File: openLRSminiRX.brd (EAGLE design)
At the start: 20.2 x 21.8 mm, 19 parts, among them U1 ATMEGA328P, U2 V_REG_LDOSMD

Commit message: update, fully routed.
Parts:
- removed C4, C9: (no value), rcl:C0805
- removed U2: V_REG_LDOSMD, SparkFun-PowerIC:SOT23-5
- added FILTER-1: LFCN-490, minicircuits:FV1206
- added IC1: MCP1703CB, linear:SOT23
- added JP10: SCL, SparkFun-Connectors:1X01
- added JP11: VCC, SparkFun-Connectors:1X01
- added JP12: SBUS, SparkFun-Connectors:1X01
- added JP13, JP14, JP8: GND, SparkFun-Connectors:1X01
- added JP3: RSSI, SparkFun-Connectors:1X01
- added JP4: PPM, SparkFun-Connectors:1X01
- added JP5: TXD, SparkFun-Connectors:1X01
- added JP6: RXD, SparkFun-Connectors:1X01
- added JP7: VIN, SparkFun-Connectors:1X01
- added JP9: SDA, SparkFun-Connectors:1X01
- added R3, R7: (no value), SparkFun-Resistors:0805
- C1, C10, C5, C6: device rcl:C0805 -> SparkFun-Capacitors:0805
- JP1: value (none) -> ANT; device SparkFun-Connectors:1X05 -> SparkFun-Connectors:1X01
- JP2: value (none) -> ANTF; device SparkFun-Connectors:1X05 -> SparkFun-Connectors:1X01
- R1, R2, R4, R5, R6: device rcl:R0805 -> SparkFun-Resistors:0805
- moved JP1 22.1 mm to (19.8, 18.0)
- moved JP2 16.0 mm to (19.8, 13.0)
- moved R4 14.7 mm to (13.0, 15.7), turned to 180 degrees
- moved C6 8.70 mm to (5.84, 14.2)
- moved C10 5.57 mm to (2.03, 2.54), turned to 270 degrees
- moved R2 4.02 mm to (17.8, 6.86)
- moved R1 3.78 mm to (17.8, 4.83)
- moved LED1 3.70 mm to (14.0, 4.83)
- moved LED2 3.21 mm to (14.0, 6.35)
- moved R6 2.90 mm to (9.40, 14.2), turned to 180 degrees
- moved Q1 2.27 mm to (8.64, 17.0), turned to 270 degrees
- moved C1 2.18 mm to (13.0, 17.5), turned to 180 degrees
- moved U$1 0.76 mm to (9.40, 10.9)
- moved R5 0.51 mm to (14.0, 8.13)
- moved U1 0.51 mm to (7.11, 7.87)
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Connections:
- removed net DTR: C9.1
- removed net N$16: C4.1, U2.4
- new net N$1: FILTER-1.1, JP1.1, U$1.1
- new net N$4: FILTER-1.3, JP2.1
- new net N$5: JP4.1, R7.1
- net GND: now also FILTER-1.2, FILTER-1.4, JP13.1, JP14.1, JP8.1; no longer C4.2, U2.2
- net N$10: now also R3.2
- net N$18: no longer C9.2
- net PPM: now also R7.2
- net RSSI: now also JP3.1
- net RXD: now also JP6.1
- net SBUS: now also JP12.1
- net SCL: now also JP10.1; no longer JP2.2
- net SDA: now also JP9.1; no longer JP2.3
- net TXD: now also JP5.1
- net VCC: now also IC1.2, JP11.1, R3.1; no longer JP2.1, U2.5
- net VIN: now also IC1.3, JP7.1; no longer U2.1, U2.3
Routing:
- net VCC: track 0.00 -> 48.1 mm, vias 0 -> 4
- net TXD: track 0.00 -> 33.4 mm, vias 0 -> 3
- net N$17: track 0.00 -> 17.4 mm, vias 0 -> 2
- net N$10: track 0.00 -> 14.6 mm, vias 0 -> 1
- net PPM: track 0.00 -> 14.0 mm
- net N$11: track 0.00 -> 13.0 mm, vias 0 -> 3
- net SCL: track 0.00 -> 10.5 mm, vias 0 -> 1
- net RXD: track 0.00 -> 10.1 mm, vias 0 -> 1
- net N$3: track 0.00 -> 9.38 mm
- net SBUS: track 0.00 -> 8.38 mm
- net N$9: track 0.00 -> 8.22 mm, vias 0 -> 1
- net N$19: track 0.00 -> 7.89 mm, vias 0 -> 2
- net SDA: track 0.00 -> 7.15 mm, vias 0 -> 1
- net RSSI: track 0.00 -> 5.74 mm
- net N$2: track 0.00 -> 5.64 mm
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- added copper zone on layer 1, net GND
- added copper zone on layer 16, net GND
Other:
- board size 20.2 x 21.8 mm -> 21.3 x 21.8 mm

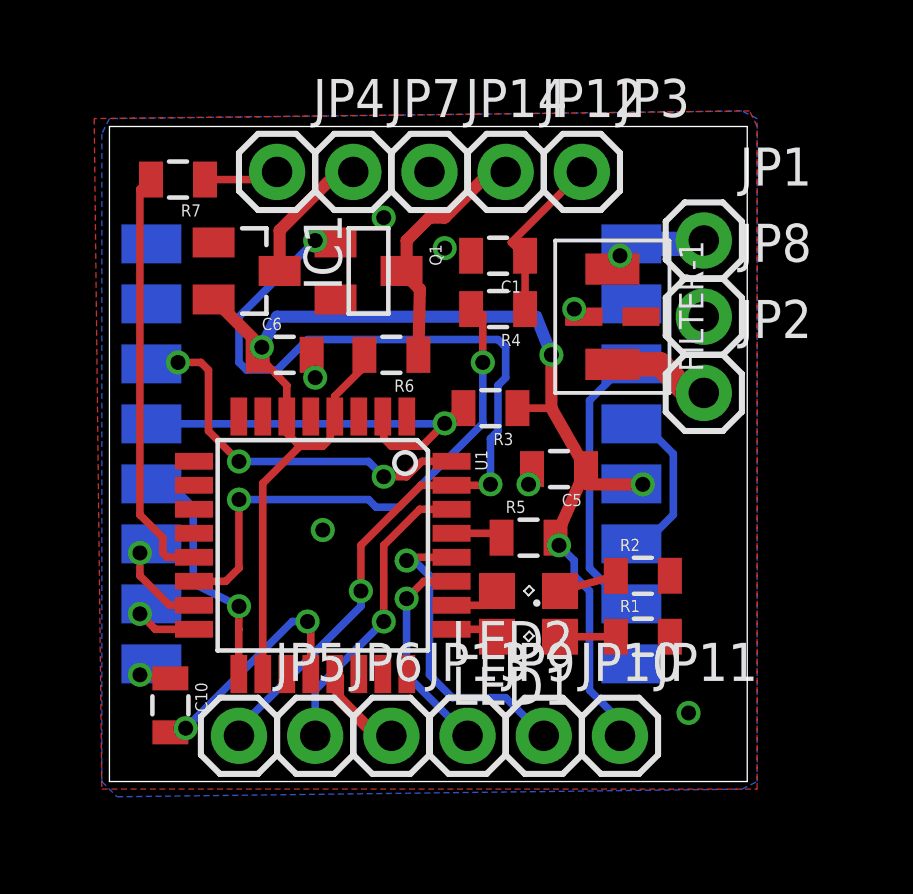
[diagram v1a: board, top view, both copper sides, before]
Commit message: updates (fix RSSI output pin)
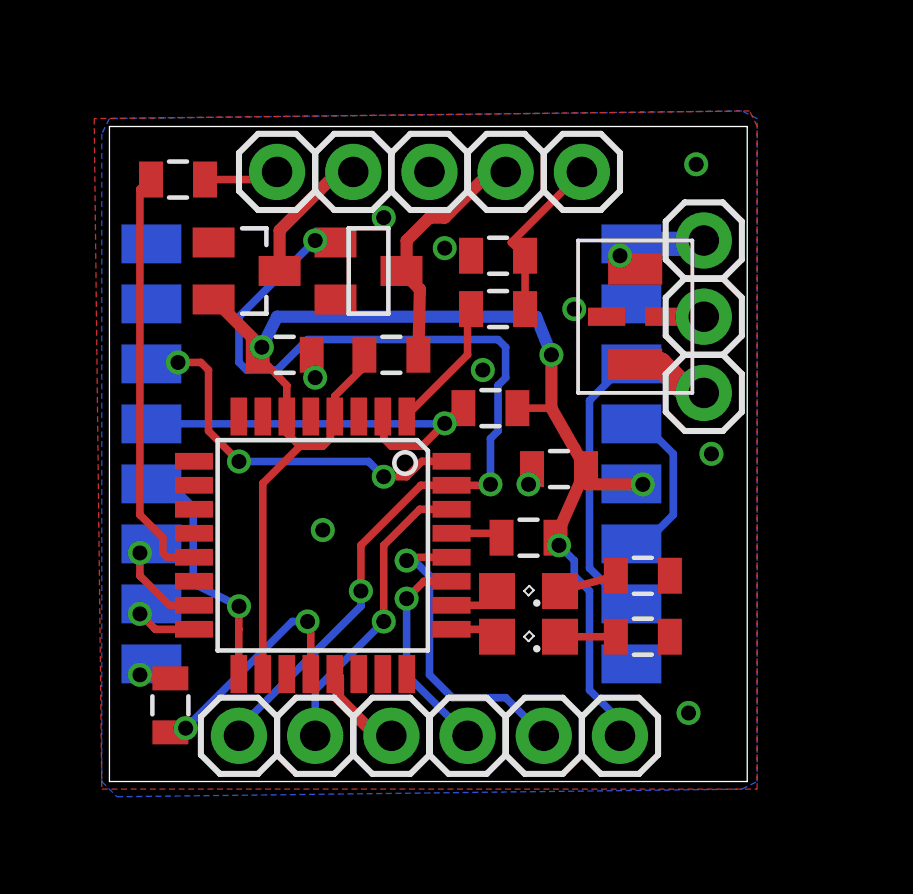
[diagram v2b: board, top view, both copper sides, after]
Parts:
- moved FILTER-1 0.76 mm to (17.5, 15.5)
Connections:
- removed net N$17: R4.2, U1.14
- new net N$6: R4.2, U1.1
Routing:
- net N$17: track 17.4 -> 0.00 mm, vias 2 -> 0
- net N$6: track 0.00 -> 4.47 mm
- net N$4: track 3.44 -> 2.68 mm
- net GND: vias 8 -> 11

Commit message: cleanups
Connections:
- net GND: now also IC1.1
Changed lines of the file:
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@@
 <via x="20.066" y="10.922" extent="1-16" drill="0.5"/>
 <via x="19.558" y="20.574" extent="1-16" drill="0.5"/>
+<contactref element="IC1" pad="1"/>
 </signal>
 <signal name="N$2">

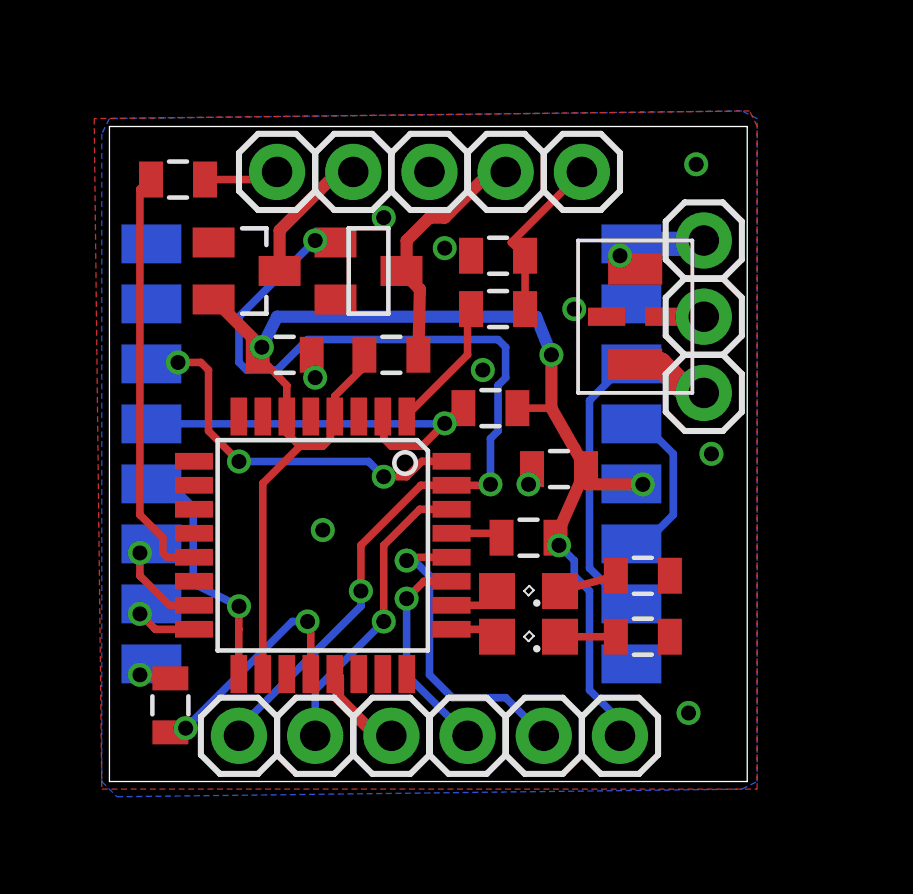
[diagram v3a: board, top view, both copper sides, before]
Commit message: Connect ICP to PPM (allow TX operation like on 6ch)
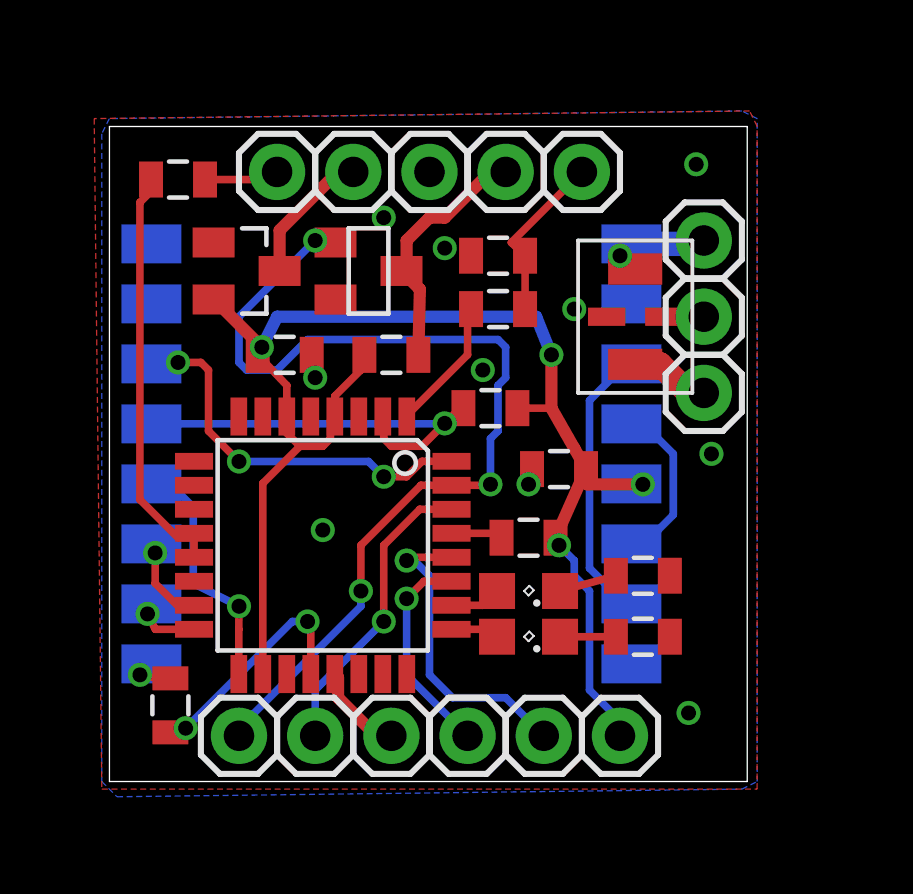
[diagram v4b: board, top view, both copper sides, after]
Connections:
- net PPM: now also U1.12
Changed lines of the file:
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@@
 <contactref element="U1" pad="15"/>
 <contactref element="U$1" pad="11"/>
-<wire x1="2.8194" y1="5.874" x2="2" y2="5.874" width="0.254" layer="1"/>
-<wire x1="2" y1="5.874" x2="1.016" y2="6.858" width="0.254" layer="1"/>
-<wire x1="1.016" y1="6.858" x2="1.016" y2="7.62" width="0.254" layer="1"/>
-<via x="1.016" y="7.62" extent="1-16" drill="0.5"/>
-<wire x1="1.016" y1="7.62" x2="1.096" y2="7.62" width="0.254" layer="16"/>
+<wire x1="2.8194" y1="5.874" x2="2.254" y2="5.874" width="0.254" layer="1"/>
+<wire x1="2.254" y1="5.874" x2="1.524" y2="6.604" width="0.254" layer="1"/>
+<wire x1="1.524" y1="6.604" x2="1.524" y2="7.62" width="0.254" layer="1"/>
+<via x="1.524" y="7.62" extent="1-16" drill="0.5"/>
+<wire x1="1.524" y1="7.62" x2="1.096" y2="7.62" width="0.254" layer="16"/>
 <wire x1="1.096" y1="7.62" x2="1.398" y2="7.922" width="0.254" layer="16"/>
 </signal>
@@
 <contactref element="U$1" pad="10"/>
 <wire x1="2.8194" y1="5.074" x2="1.53" y2="5.074" width="0.254" layer="1"/>
-<wire x1="1.53" y1="5.074" x2="1.016" y2="5.588" width="0.254" layer="1"/>
-<via x="1.016" y="5.588" extent="1-16" drill="0.5"/>
-<wire x1="1.016" y1="5.588" x2="1.064" y2="5.588" width="0.254" layer="16"/>
+<wire x1="1.53" y1="5.074" x2="1.27" y2="5.588" width="0.254" layer="1"/>
+<via x="1.27" y="5.588" extent="1-16" drill="0.5"/>
+<wire x1="1.27" y1="5.588" x2="1.064" y2="5.588" width="0.254" layer="16"/>
 <wire x1="1.064" y1="5.588" x2="1.398" y2="5.922" width="0.254" layer="16"/>
 </signal>
@@
 <signal name="PPM">
 <contactref element="U1" pad="13"/>
-<wire x1="2.8194" y1="7.474" x2="1.924" y2="7.474" width="0.254" layer="1"/>
-<wire x1="1.924" y1="7.474" x2="1.778" y2="7.62" width="0.254" layer="1"/>
-<wire x1="1.778" y1="7.62" x2="1.778" y2="8.128" width="0.254" layer="1"/>
-<wire x1="1.778" y1="8.128" x2="1.016" y2="8.89" width="0.254" layer="1"/>
-<wire x1="1.016" y1="8.89" x2="1.016" y2="19.746" width="0.254" layer="1"/>
 <contactref element="R7" pad="2"/>
-<wire x1="1.016" y1="19.746" x2="1.386" y2="20.066" width="0.254" layer="1"/>
+<contactref element="U1" pad="12"/>
+<wire x1="1.386" y1="20.066" x2="1.386" y2="19.674" width="0.254" layer="1"/>
+<wire x1="1.386" y1="19.674" x2="1.016" y2="19.304" width="0.254" layer="1"/>
+<wire x1="1.016" y1="19.304" x2="1.016" y2="9.398" width="0.254" layer="1"/>
+<wire x1="1.016" y1="9.398" x2="2.286" y2="8.128" width="0.254" layer="1"/>
+<wire x1="2.286" y1="8.128" x2="2.6734" y2="8.128" width="0.254" layer="1"/>
+<wire x1="2.6734" y1="8.128" x2="2.8194" y2="8.274" width="0.254" layer="1"/>
+<wire x1="2.8194" y1="8.274" x2="2.8194" y2="7.474" width="0.254" layer="1"/>
 </signal>
 <signal name="RSSI">

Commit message: add resonator (optional)
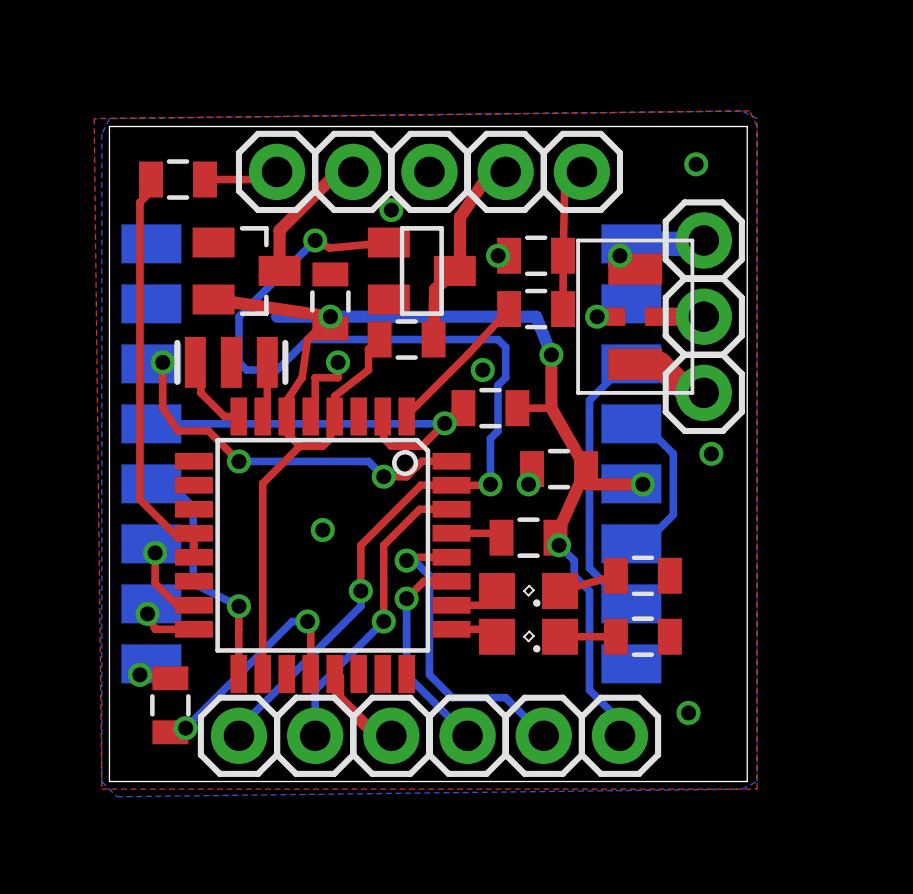
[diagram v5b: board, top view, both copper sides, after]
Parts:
- added Y1: 16MHz, SparkFun-FreqCtrl:RESONATOR-SMD
- moved C6 2.34 mm to (7.37, 16.0), turned to 90 degrees
- moved Q1 1.78 mm to (10.4, 17.0)
- moved C1 1.27 mm to (14.2, 17.5)
- moved R4 1.27 mm to (14.2, 15.7)
- moved R6 0.72 mm to (9.91, 14.7)
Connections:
- new net N$16: U1.7, Y1.1
- new net N$17: U1.8, Y1.3
- net GND: now also Y1.2
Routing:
- net GND: track 4.71 -> 7.43 mm
- net N$17: track 0.00 -> 2.68 mm
- net VCC: track 48.1 -> 50.5 mm
- net N$16: track 0.00 -> 1.96 mm
- net TXD: track 33.4 -> 35.1 mm
- net SBUS: track 8.38 -> 6.76 mm
- net RSSI: track 5.74 -> 4.81 mm
- net N$6: track 4.47 -> 5.35 mm
